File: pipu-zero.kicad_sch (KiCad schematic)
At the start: 0 parts

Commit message: add cc1101 library
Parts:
- added J1: USB_C_Receptacle_USB2.0_14P, symbol Connector:USB_C_Receptacle_USB2.0_14P
- added U1: ESP32-S3-WROOM-1, RF_Module:ESP32-S3-WROOM-1, symbol RF_Module:ESP32-S3-WROOM-1
- added U2: CC1101, CC1101:QLP20, symbol CC1101:CC1101
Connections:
- new net: U1.1 (GND), U1.40 (GND), U1.41 (GND)
- new net: J1.A1 (GND), J1.A12 (GND), J1.B1 (GND), J1.B12 (GND)
- new net: J1.A4 (VBUS), J1.A9 (VBUS), J1.B4 (VBUS), J1.B9 (VBUS)

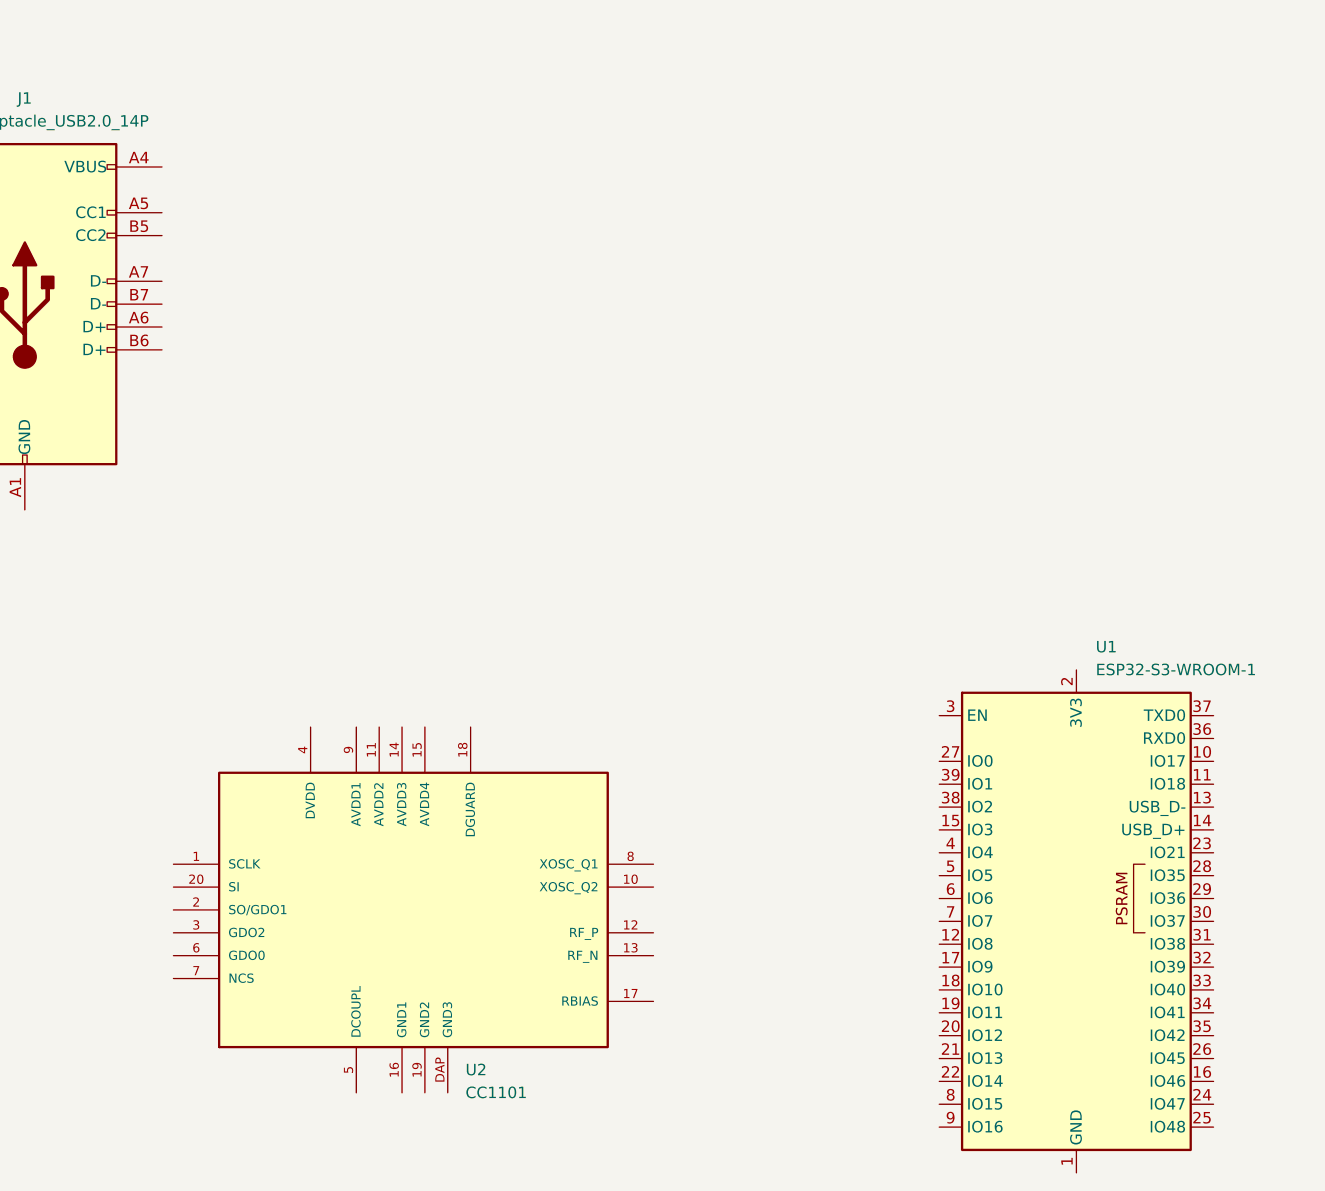
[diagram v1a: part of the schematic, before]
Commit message: add libraries to kicad
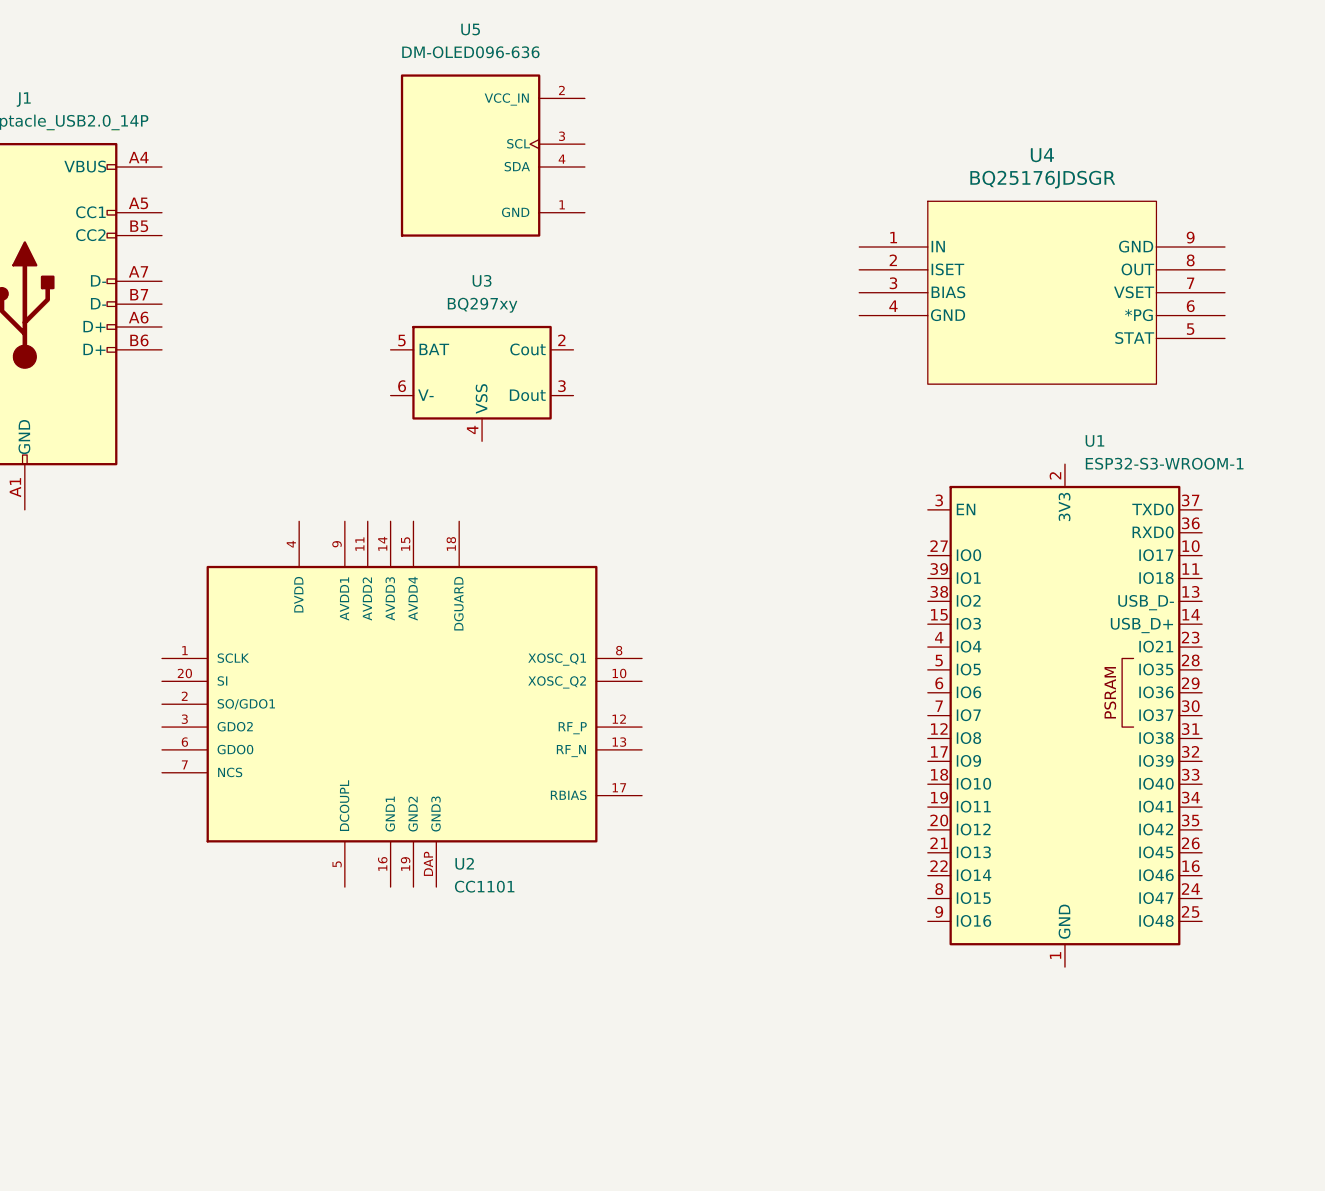
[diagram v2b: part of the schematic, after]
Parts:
- added U3: BQ297xy, Package_SON:WSON-6_1.5x1.5mm_P0.5mm, symbol Battery_Management:BQ297xy
- added U4: BQ25176JDSGR, WSON_MDSGR_TEX, symbol 2025-10-25_14-37-11:BQ25176JDSGR
- added U5: DM-OLED096-636, oled_128x64:MODULE_DM-OLED096-636, symbol DM-OLED096-636:DM-OLED096-636
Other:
- moved on the sheet: U1, U2

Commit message: initial schematic
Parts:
- removed U1: ESP32-S3-WROOM-1, RF_Module:ESP32-S3-WROOM-1, symbol RF_Module:ESP32-S3-WROOM-1
- removed U2: CC1101, CC1101:QLP20, symbol CC1101:CC1101
- removed U3: BQ297xy, Package_SON:WSON-6_1.5x1.5mm_P0.5mm, symbol Battery_Management:BQ297xy
- removed U4: BQ25176JDSGR, WSON_MDSGR_TEX, symbol 2025-10-25_14-37-11:BQ25176JDSGR
- removed U5: DM-OLED096-636, oled_128x64:MODULE_DM-OLED096-636, symbol DM-OLED096-636:DM-OLED096-636
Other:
- added sheet I-O (in_out.kicad_sch)
- added sheet Infrared (infrared.kicad_sch)
- added sheet MCU (mcu.kicad_sch)
- added sheet Power Manager (pwr-management.kicad_sch)
- added sheet Radio (radio.kicad_sch)
- moved on the sheet: J1

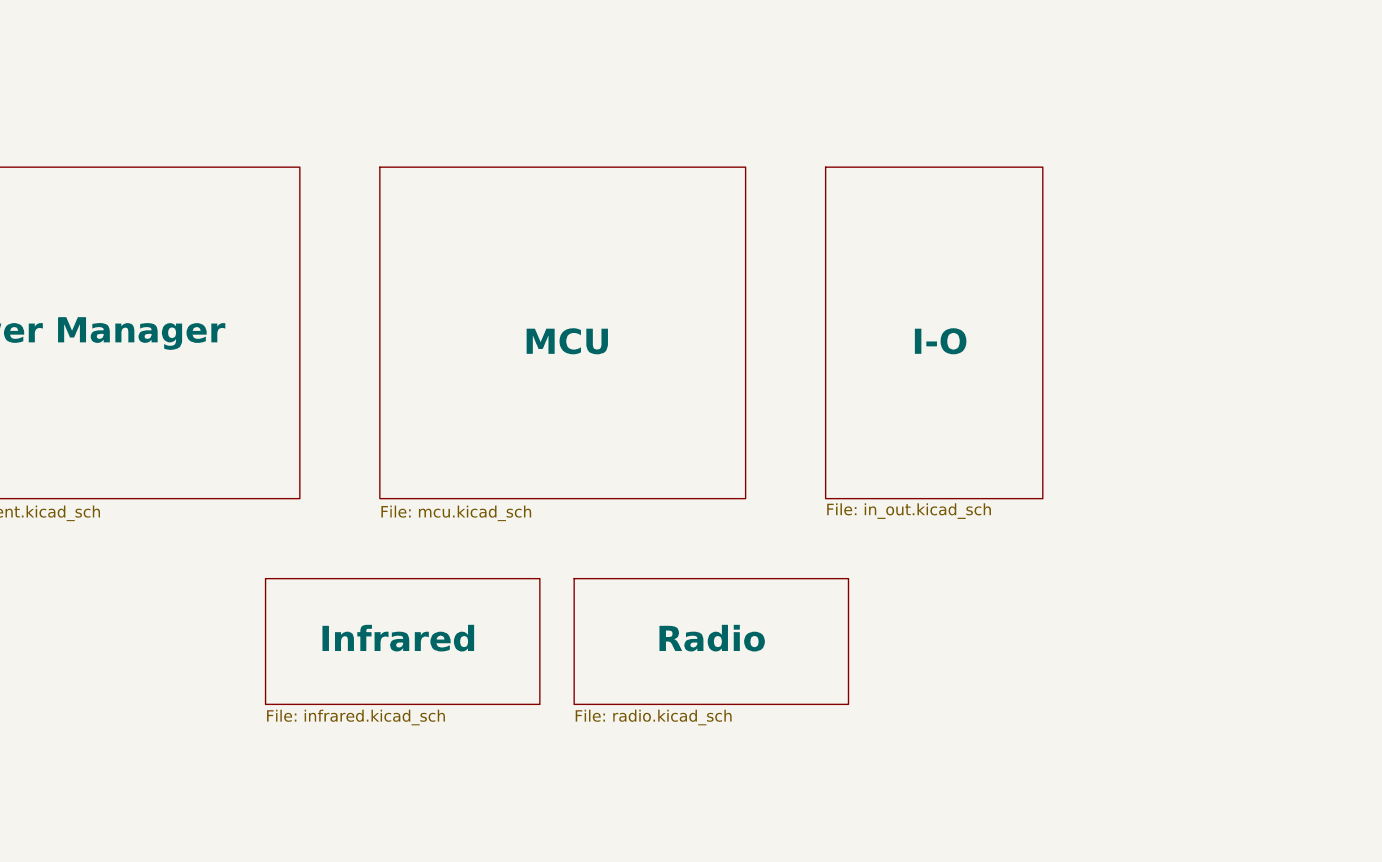
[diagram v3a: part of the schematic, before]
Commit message: component placement inside schematic
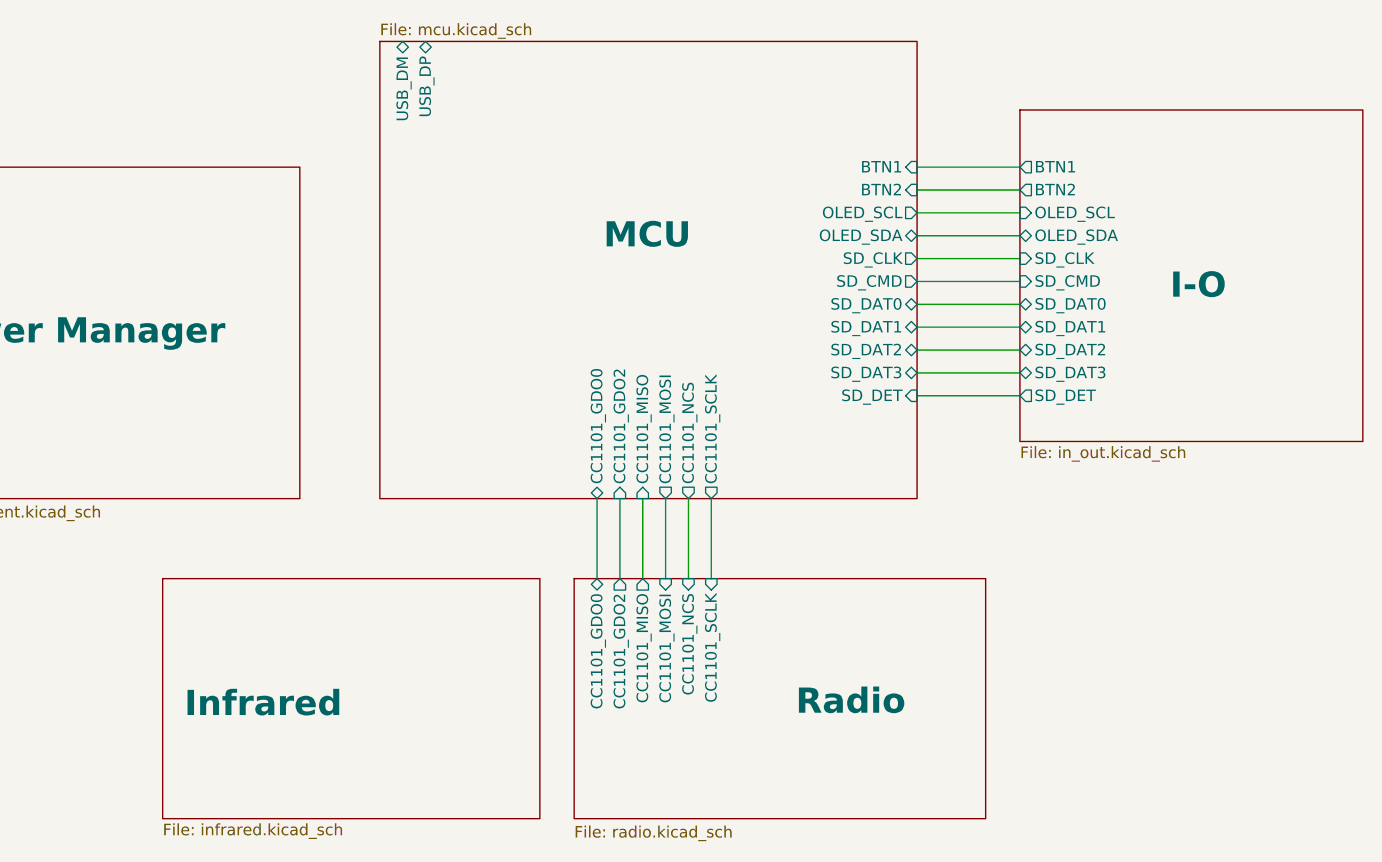
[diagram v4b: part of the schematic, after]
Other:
- sheet I-O ports: added BTN1, BTN2, OLED_SCL, OLED_SDA, SD_CLK, SD_CMD, SD_DAT0, SD_DAT1, SD_DAT2, SD_DAT3, SD_DET; removed none
- sheet MCU ports: added BTN1, BTN2, CC1101_GDO0, CC1101_GDO2, CC1101_MISO, CC1101_MOSI, CC1101_NCS, CC1101_SCLK, OLED_SCL, OLED_SDA, SD_CLK, SD_CMD, SD_DAT0, SD_DAT1, SD_DAT2, SD_DAT3, SD_DET, USB_DM, USB_DP; removed none
- sheet Radio ports: added CC1101_GDO0, CC1101_GDO2, CC1101_MISO, CC1101_MOSI, CC1101_NCS, CC1101_SCLK; removed none

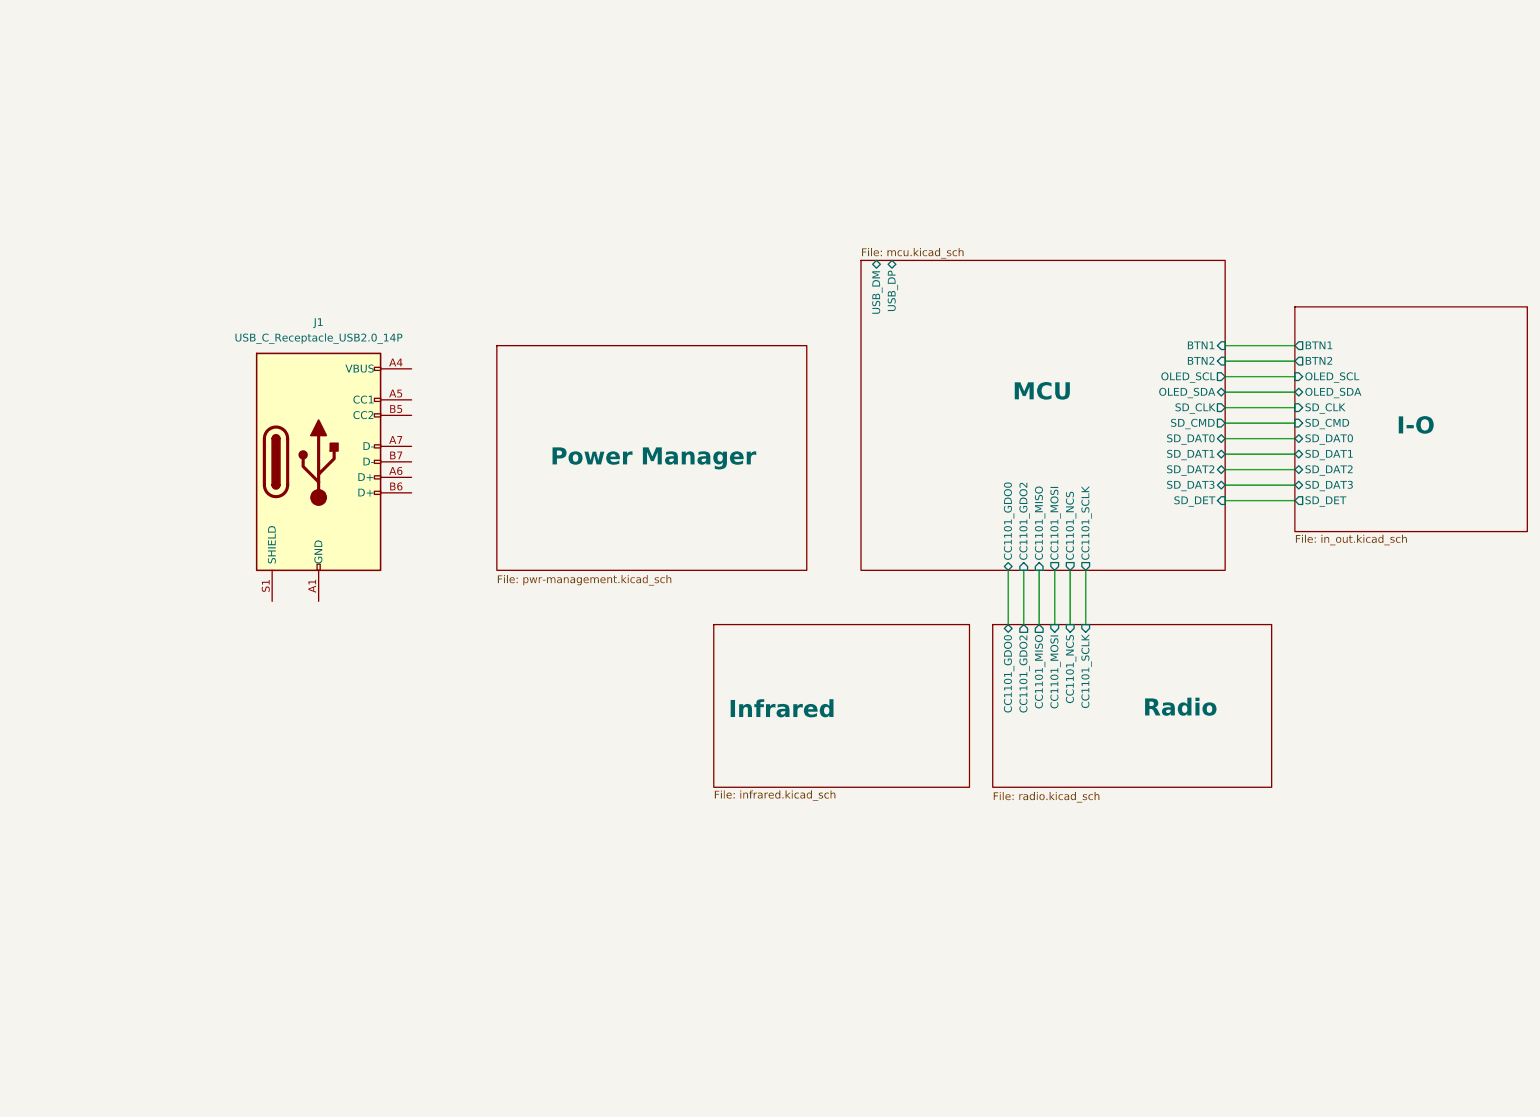
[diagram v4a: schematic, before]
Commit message: add esd usb protections
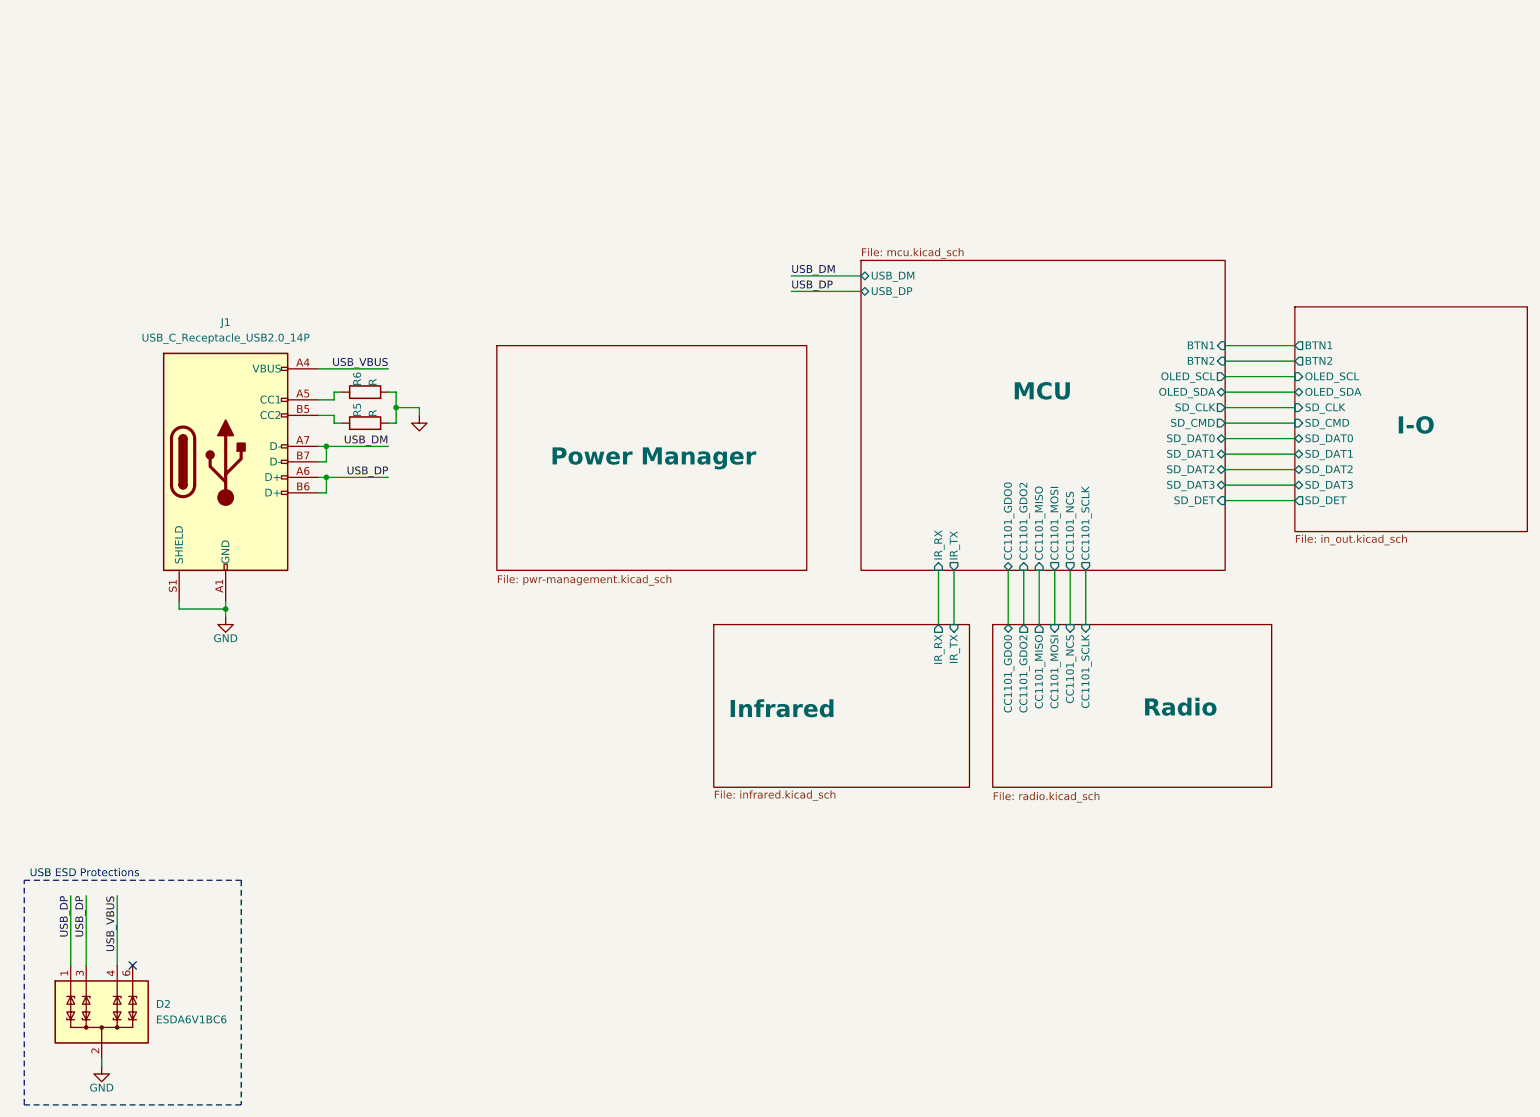
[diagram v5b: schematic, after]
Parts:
- added D2: ESDA6V1BC6, Package_TO_SOT_SMD:SOT-23-6, symbol Power_Protection:ESDA6V1BC6
- added R5, R6: R, symbol Device:R
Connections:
- net GND: now reaches J1.A1 (GND), J1.A12 (GND), J1.B1 (GND), J1.B12 (GND)
- net GND: now also J1.S1 (SHIELD), D2.2 (COM), D2.5 (COM), R5.2, R6.2
- net USB_VBUS: now reaches J1.A4 (VBUS), J1.A9 (VBUS), J1.B4 (VBUS), J1.B9 (VBUS)
- net USB_VBUS: now also D2.4 (TVS3)
- net at J1.A5 (CC1): now also R6.1
- net USB_DP: now reaches J1.A6 (D+)
- net USB_DP: now also J1.B6 (D+), D2.1 (TVS1), D2.3 (TVS2)
- net USB_DM: now reaches J1.A7 (D-)
- net USB_DM: now also J1.B7 (D-)
- net at J1.B5 (CC2): now also R5.1
- no-connect marks 0 -> 1
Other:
- sheet Infrared ports: added IR_RX, IR_TX; removed none
- sheet MCU ports: added IR_RX, IR_TX; removed none
- note added: "USB ESD Protections"
- moved on the sheet: J1
